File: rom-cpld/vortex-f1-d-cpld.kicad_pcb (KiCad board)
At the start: 2 copper layers, 92.5 x 50 mm, 47 parts, among them J1 JTAG, U1 FDC 9229, U2 XC9572XL, U3 AZ1117-3.3, U4 uPD765AC, U5 AM29F010, U6 74LS06N, U7 SN74LS07N, U8 74LS06N, X1 8Mhz

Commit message: Save work
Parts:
- removed JP1: ~{VORTEX}/CPC, Jumper:SolderJumper-2_P1.3mm_Open_RoundedPad1.0x1.5mm
- added R21: 680, Resistor_SMD:R_0603_1608Metric_Pad0.98x0.95mm_HandSolder, B.Cu at (148.6, 97.0)
- added SW1: SW_DIP_x04, Button_Switch_THT:SW_DIP_SPSTx04_Slide_6.7x11.72mm_W7.62mm_P2.54mm_LowProfile, F.Cu at (120.3, 101.0)
- moved X1 15.5 mm to (135.2, 116.1)
- moved C11 14.1 mm to (116.6, 130.5)
- moved R3 14.1 mm to (121.5, 123.8)
- moved U1 14.1 mm to (126.3, 131.4)
- moved R13 14.1 mm to (123.4, 131.4)
- moved R2 14.1 mm to (121.5, 126.4)
- moved C1 1.76 mm to (140.5, 128.8)
- moved C2 1.76 mm to (140.5, 125.3)
- moved U3 1.76 mm to (133.8, 127.1)
- moved D1 1.41 mm to (131.9, 132.7)
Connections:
- U2 pad 12: unconnected-(U2-Pad12) -> SW1
- U2 pad 13: unconnected-(U2-Pad13) -> SW2
- U2 pad 16: ~{VORTEX}/CPC -> SW3
- U2 pad 19: unconnected-(U2-Pad19) -> SW4
- U2 pad 33: A0 -> /A15
- U2 pad 34: /A1 -> /A13
- U2 pad 35: /A2 -> /A10
- U2 pad 36: /A3 -> /A7
- U2 pad 38: /A4 -> /A6
- U2 pad 40: /A6 -> /A4
- U2 pad 42: /A7 -> /A3
- U2 pad 43: /A10 -> /A2
- U2 pad 44: /A13 -> /A1
- U2 pad 45: /A15 -> A0
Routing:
- net +5V: track 307.9 -> 0.00 mm, vias 28 -> 0
- net +3.3V: track 160.5 -> 4.95 mm, vias 10 -> 0
- net GND: track 104.7 -> 0.00 mm, vias 33 -> 0
- net WDATA': track 90.3 -> 0.00 mm, vias 4 -> 0
- net RDATA': track 86.3 -> 0.00 mm, vias 6 -> 0
- net DIR: track 81.8 -> 0.00 mm, vias 2 -> 0
- net D0: track 69.8 -> 0.00 mm, vias 7 -> 0
- net Net-(U1-Pad5): track 67.2 -> 0.00 mm, vias 3 -> 0
- net Net-(U1-Pad8): track 64.7 -> 0.00 mm, vias 3 -> 0
- net CLK4: track 64.7 -> 0.00 mm, vias 1 -> 0
- net Net-(D1-Pad2): track 64.5 -> 0.00 mm, vias 4 -> 0
- net Net-(U1-Pad6): track 62.5 -> 0.00 mm, vias 3 -> 0
- net MFM: track 60.7 -> 0.00 mm, vias 3 -> 0
- net Net-(U1-Pad9): track 59.8 -> 0.00 mm, vias 1 -> 0
- net WPT: track 56.1 -> 0.00 mm, vias 3 -> 0
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
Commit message: Save CPLD work
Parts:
- removed C10, C11, C9: 100n, Capacitor_SMD:C_0603_1608Metric_Pad1.08x0.95mm_HandSolder
- removed R10, R11, R12, R7, R8, R9: 10k, Resistor_SMD:R_0603_1608Metric_Pad0.98x0.95mm_HandSolder
- removed R13, R14, R15, R16, R17, R18, R19, R20, R21: 680, Resistor_SMD:R_0603_1608Metric_Pad0.98x0.95mm_HandSolder
- removed S2: FD Bus, Connector_IDC:IDC-Header_2x17_P2.54mm_Horizontal
- removed U4: uPD765AC, Package_DIP:DIP-40_W15.24mm_Socket
- removed U6, U8: 74LS06N, Package_SO:SSOP-14_5.3x6.2mm_P0.65mm
- removed U7: SN74LS07N, Package_SO:SSOP-14_5.3x6.2mm_P0.65mm
- removed X1: 8Mhz, Oscillator:Oscillator_SMD_EuroQuartz_XO91-4Pin_7.0x5.0mm
- added C13: 15pF, Capacitor_SMD:C_0603_1608Metric_Pad1.08x0.95mm_HandSolder, F.Cu at (81.5, 107.8)
- added C14: 47pF, Capacitor_SMD:C_0603_1608Metric_Pad1.08x0.95mm_HandSolder, F.Cu at (117.1, 80.9)
- added J2: Floppy, Connector_PinHeader_2.54mm:PinHeader_2x17_P2.54mm_Horizontal, F.Cu at (200.8, 94.2)
- added Y1: 16MHz, Crystal:Crystal_HC49-U_Horizontal, F.Cu at (119.6, 62.8)
- C1, C12, C2, C3, C4, C5, C6, C7, C8, D1, R1, R2, R3, R4, U2, U3: moved to F.Cu
- R5, R6: value 10k -> 1k; moved to F.Cu
- U1: value FDC 9229 -> 37C65; footprint Package_DIP:DIP-20_W7.62mm_Socket -> Package_LCC:PLCC-44
- U5: footprint Package_LCC:PLCC-32_THT-Socket -> Package_LCC:PLCC-32_11.4x14.0mm_P1.27mm
- moved R4 73.0 mm to (101.8, 84.7), turned to 0 degrees
- moved C7 71.4 mm to (116.6, 119.9)
- moved C8 71.4 mm to (116.6, 110.0)
- moved C4 61.8 mm to (121.4, 122.1), turned to 180 degrees
- moved U1 60.0 mm to (179.1, 102.8), turned to 0 degrees
- moved R5 56.6 mm to (97.5, 82.2), turned to 0 degrees
- moved R6 55.0 mm to (101.8, 82.2), turned to 0 degrees
- moved C5 55.0 mm to (124.9, 128.3)
- moved R1 53.4 mm to (139.8, 94.4), turned to 180 degrees
- moved R2 48.1 mm to (97.5, 84.7)
- moved D1 41.0 mm to (172.8, 132.7), turned to 180 degrees
- moved C3 39.5 mm to (132.6, 112.9)
- moved R3 39.1 mm to (85.9, 107.8)
- moved C6 28.0 mm to (138.4, 122.1), turned to 0 degrees
- moved U5 21.9 mm to (153.4, 102.0)
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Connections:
- R2 pad 1: Net-(R2-Pad1) -> /~{DC}
- R2 pad 2: +5V -> VCC
- R3 pad 1: Net-(R3-Pad1) -> /~{RDATA}
- R3 pad 2: +5V -> VCC
- R4 pad 1: Net-(R4-Pad1) -> /~{WP}
- R4 pad 2: +5V -> VCC
- R5 pad 1: D0 -> /~{TRK0}
- R5 pad 2: +5V -> VCC
- R6 pad 1: /D1 -> /~{INDEX}
- R6 pad 2: +5V -> VCC
- U1 pad 1: RDATA' -> ~{IORD}
- U1 pad 10: GND -> /D3
- U1 pad 11: ~{CLKIN} -> /D4
- U1 pad 12: Net-(U1-Pad12) -> /D5
- U1 pad 13: Net-(U1-Pad13) -> /D6
- U1 pad 14: Net-(U1-Pad14) -> /D7
- U1 pad 16: +5V -> unconnected-(U1-Pad16)
- U1 pad 17: Net-(R3-Pad1) -> GND
- U1 pad 18: Net-(R2-Pad1) -> /~{DOR_WR}
- U1 pad 19: GND -> /~{CCR_WR}
- U1 pad 2: +5V -> ~{IOWR}
- U1 pad 20: +5V -> RESET
- U1 pad 3: GND -> ~{FDCCS}
- U1 pad 4: MFM -> A0
- U1 pad 5: Net-(U1-Pad5) -> VCC
- U1 pad 6: Net-(U1-Pad6) -> VCC
- U1 pad 7: WDATA' -> D0
- U1 pad 8: Net-(U1-Pad8) -> /D1
- U1 pad 9: Net-(U1-Pad9) -> /D2
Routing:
- net A0: track 20.8 -> 0.00 mm, vias 2 -> 0
- net /A1: track 18.4 -> 0.00 mm, vias 2 -> 0
- net /A2: track 17.6 -> 0.00 mm, vias 2 -> 0
- net /A4: track 17.6 -> 0.00 mm, vias 2 -> 0
- net /A3: track 17.0 -> 0.00 mm, vias 2 -> 0
- net /A6: track 16.1 -> 0.00 mm, vias 2 -> 0
- net /A5: track 15.8 -> 0.00 mm, vias 2 -> 0
- net /A7: track 14.6 -> 0.00 mm, vias 2 -> 0
- net /A10: track 11.7 -> 0.00 mm
- net /A15: track 9.56 -> 0.00 mm
- net /A13: track 8.71 -> 0.00 mm
- net +3.3V: track 4.95 -> 0.00 mm
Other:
- board text removed: "8x10k"

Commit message: v1.0 sent to jlcpcb for production
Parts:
- removed SW1: SW_DIP_x04, Button_Switch_THT:SW_DIP_SPSTx04_Slide_6.7x11.72mm_W7.62mm_P2.54mm_LowProfile
- added REF**: DIP-40_W15.24mm_Socket, Package_DIP:DIP-40_W15.24mm_Socket, F.Cu at (120.7, 109.7)
- Y1: footprint Crystal:Crystal_HC49-U_Horizontal -> Crystal:Crystal_SMD_7050-4Pin_7.0x5.0mm
- moved R1 26.1 mm to (156.1, 114.8)
- moved U5 21.4 mm to (148.1, 122.7)
- moved U3 20.5 mm to (122.8, 115.2)
- moved C12 9.10 mm to (132.9, 120.9)
- moved C6 9.10 mm to (129.6, 119.5)
- moved U1 8.39 mm to (187.5, 102.9)
- moved D1 8.36 mm to (181.1, 131.3)
- moved U2 5.36 mm to (168.7, 122.4)
- moved C3 3.94 mm to (133.9, 116.6)
- moved LED1 2.76 mm to (194.1, 91.7)

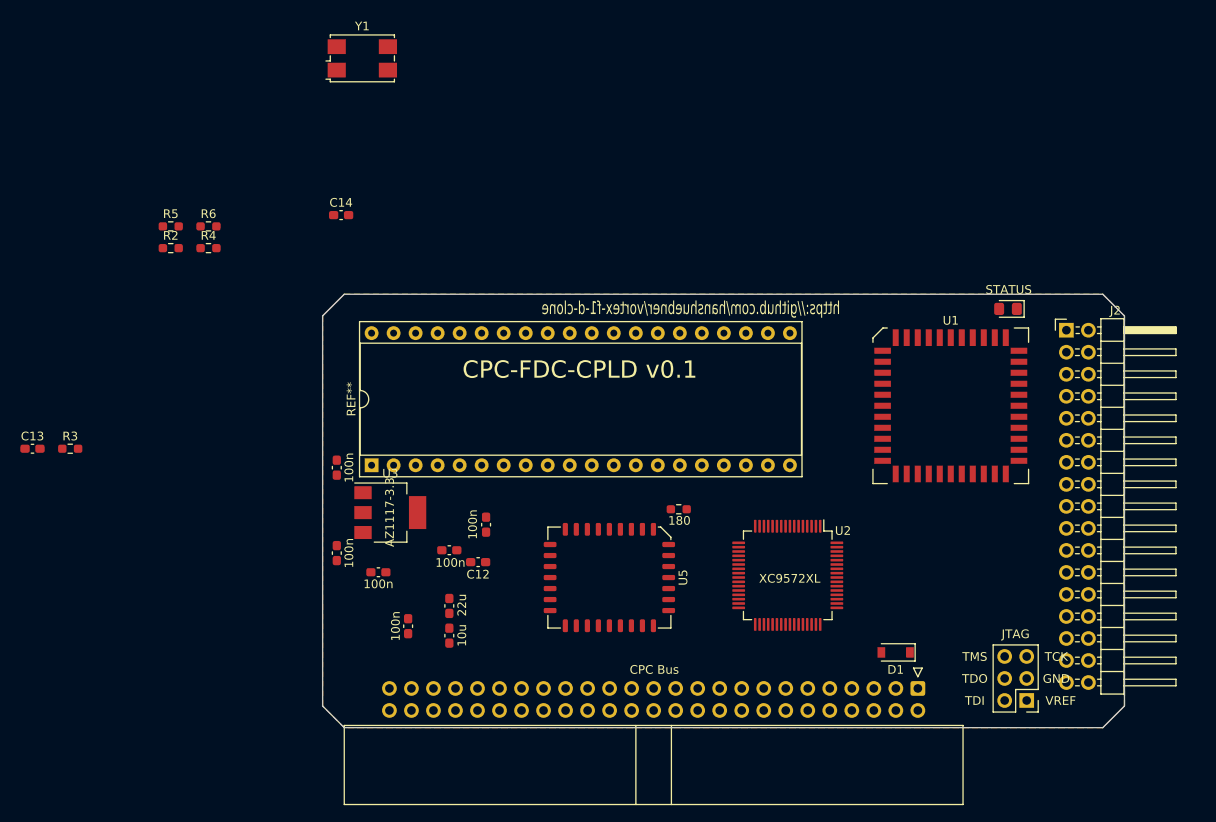
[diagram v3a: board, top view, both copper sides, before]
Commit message: add new vhdl code
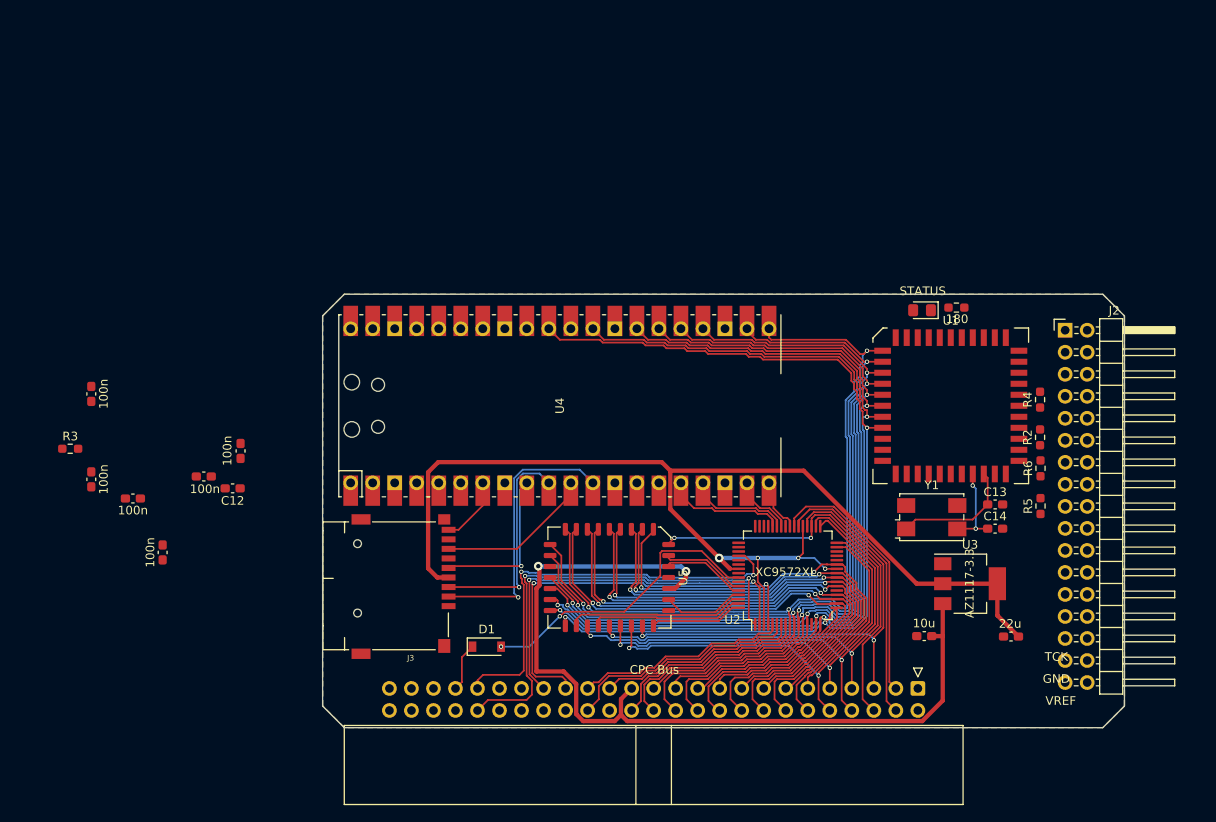
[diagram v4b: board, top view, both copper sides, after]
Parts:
- removed J1: JTAG, Connector_PinHeader_2.54mm:PinHeader_2x03_P2.54mm_Vertical
- removed REF**: DIP-40_W15.24mm_Socket, Package_DIP:DIP-40_W15.24mm_Socket
- added J3: Micro_SD_Card, project:J_SD_Card-micro_socket_A, F.Cu at (122.5, 122.8)
- added U4: Pico, MCU_RaspberryPi_and_Boards:RPi_Pico_SMD_TH, F.Cu at (142.4, 102.9)
- R2, R3, R4, R5, R6: value 1k -> 150
- moved C13 111.2 mm to (192.6, 114.2)
- moved R5 105.4 mm to (197.8, 114.4), turned to 90 degrees
- moved R2 102.6 mm to (197.8, 106.5), turned to 90 degrees
- moved R6 100.0 mm to (197.8, 110.1), turned to 90 degrees
- moved R4 97.5 mm to (197.8, 102.2), turned to 90 degrees
- moved Y1 84.4 mm to (185.3, 115.7)
- moved C14 83.7 mm to (192.6, 117.0)
- moved U3 67.4 mm to (189.7, 123.4)
- moved C2 64.9 mm to (194.4, 129.5), turned to 180 degrees
- moved C1 54.8 mm to (184.4, 129.4), turned to 180 degrees
- moved D1 47.2 mm to (133.9, 130.7), turned to 0 degrees
- moved R1 39.6 mm to (188.1, 91.5)
- moved C6 29.6 mm to (101.3, 111.0)
- moved C12 29.6 mm to (104.6, 112.4)
- moved C3 29.6 mm to (105.5, 108.1)
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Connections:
- net /~{CCR_WR} renamed ~{LDCR}
- net /~{DOR_WR} renamed ~{LDOR}
- S1 pad 26: D0 -> /D0
- S1 pad 29: /~{M1} -> ~{M1}
- S1 pad 35: /~{INT} -> ~{INT}
- S1 pad 39: READY -> /READY
- U1 pad 7: D0 -> /D0
- U2 pad 1: ~{RW}/SEEK -> ~{ROMEN}
- U2 pad 10: ~{IOWR} -> /D1
- U2 pad 11: ~{FDCCS} -> /D2
- U2 pad 12: SW1 -> /D3
- U2 pad 13: SW2 -> /D4
- U2 pad 15: LED1 -> /D5
- U2 pad 16: SW3 -> /D6
- U2 pad 17: A9 -> /D7
- U2 pad 18: A8 -> A0
- U2 pad 19: SW4 -> /A1
- U2 pad 2: FLTR/STEP -> ~{INT}
- U2 pad 20: STEP -> /A2
- U2 pad 22: WGATE -> /A3
- U2 pad 23: TRK00 -> /A4
- U2 pad 24: MTRON -> /A5
- U2 pad 25: ~{DS2'} -> /A6
- U2 pad 27: ~{DS1'} -> /A7
- U2 pad 31: ~{DS0'} -> A8
- U2 pad 32: ~{DS3'} -> A9
- U2 pad 33: /A15 -> /A10
- U2 pad 34: /A13 -> /A11
- U2 pad 35: /A10 -> /A12
- U2 pad 36: /A7 -> /A13
- U2 pad 38: /A6 -> /A14
- U2 pad 39: /A5 -> /A15
- U2 pad 4: FLT/TRK0 -> ~{WR}
- U2 pad 40: /A4 -> PICO15
- U2 pad 42: /A3 -> PICO14
- U2 pad 43: /A2 -> PICO13
- U2 pad 44: /A1 -> PICO12
- U2 pad 45: A0 -> PICO10
- U2 pad 46: D0 -> PICO11
- U2 pad 47: ~{MREQ} -> unconnected-(U2-P47-Pad47)
- U2 pad 48: ~{IORQ} -> unconnected-(U2-P48-Pad48)
- U2 pad 49: ~{RD} -> unconnected-(U2-P49-Pad49)
- U2 pad 5: US1 -> ~{IORQ}
- U2 pad 50: ~{WR} -> unconnected-(U2-P50-Pad50)
- U2 pad 51: READY -> unconnected-(U2-P51-Pad51)
- U2 pad 52: ~{ROMEN} -> ~{RSET}
- U2 pad 56: ~{RSET} -> unconnected-(U2-P56-Pad56)
- U2 pad 58: CLK4 -> unconnected-(U2-P58-Pad58)
- U2 pad 59: ROMA14 -> ROMA15
- U2 pad 6: US0 -> ~{RD}
- U2 pad 60: ~{ROMWE} -> ROMA16
- U2 pad 61: ~{ROMOE} -> ~{ROMWE}
- U2 pad 63: ROMA16 -> ~{ROMOE}
- U2 pad 64: ROMA15 -> ROMA14
- U2 pad 7: WE -> ~{M1}
- U2 pad 8: RESET -> ~{MREQ}
- U2 pad 9: ~{IORD} -> /D0
- U5 pad 13: D0 -> /D0
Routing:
- net +3.3V: track 0.00 -> 134.0 mm, vias 0 -> 4
- net /D7: track 0.00 -> 126.3 mm, vias 0 -> 3
- net /D6: track 0.00 -> 122.8 mm, vias 0 -> 3
- net /D4: track 0.00 -> 117.6 mm, vias 0 -> 3
- net /D2: track 0.00 -> 117.1 mm, vias 0 -> 3
- net /D5: track 0.00 -> 116.0 mm, vias 0 -> 3
- net /D3: track 0.00 -> 113.2 mm, vias 0 -> 3
- net /D0: track 0.00 -> 112.7 mm, vias 0 -> 3
- net /D1: track 0.00 -> 109.8 mm, vias 0 -> 3
- net +5V: track 0.00 -> 101.7 mm, vias 0 -> 2
- net A0: track 0.00 -> 61.8 mm, vias 0 -> 2
- net /A2: track 0.00 -> 59.1 mm, vias 0 -> 2
- net /A10: track 0.00 -> 59.0 mm, vias 0 -> 2
- net /A1: track 0.00 -> 56.6 mm, vias 0 -> 2
- net /A4: track 0.00 -> 56.4 mm, vias 0 -> 2
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- added copper zone on B.Cu, net SDDETECT
- added copper zone on F.Cu, net SDDETECT
- removed copper zone on F.Cu, net GND
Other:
- board text added: "FutureCard v1.0"
- board text added: "https://github.com/hanshuebner/futurecard"
- board text removed: "CPC-FDC-CPLD v0.1"
- board text removed: "TDI"
- board text removed: "TDO"
- board text removed: "TMS"
- board text removed: "https://github.com/hanshuebner/vortex-f1-d-clone"
